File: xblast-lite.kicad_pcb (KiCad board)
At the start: 2 copper layers, 52 x 50.5 mm, 30 parts, among them J1 JTAG, J2 XBOX LPC, J3 GPIO, J4 LCD, J5 PLCC-32 Socket, Q1 BC846, Q2 BC846, U1 74LVC125, U3 XC9572XL-xxVQx44, U4 TPS27081A

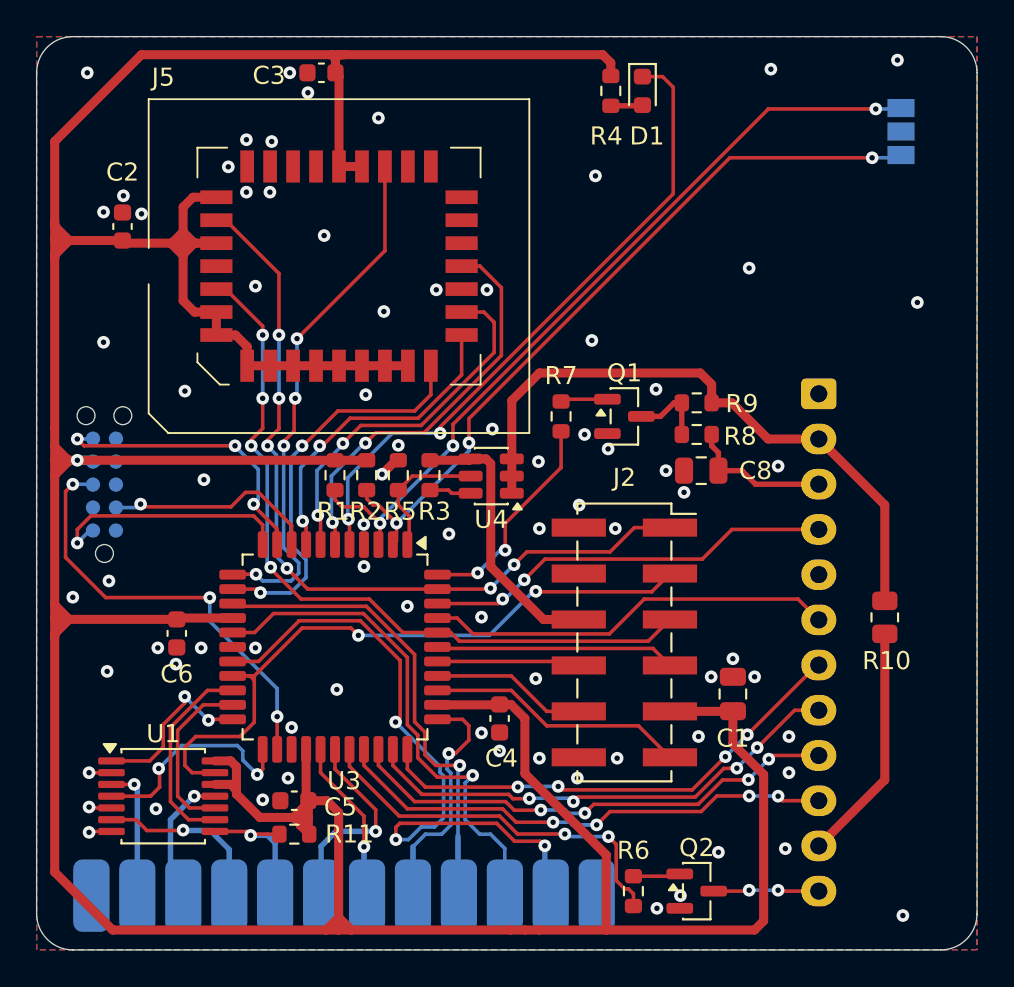
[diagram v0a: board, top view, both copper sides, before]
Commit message: Add teardrops
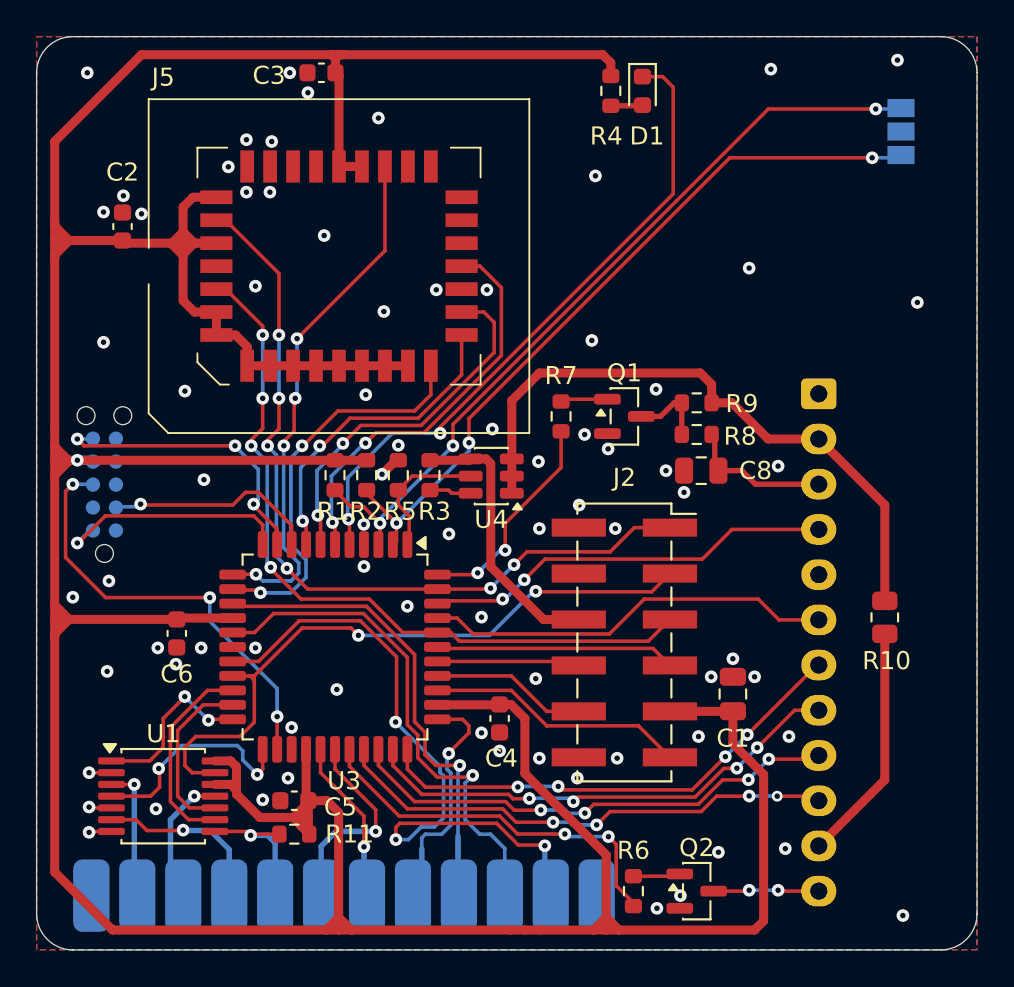
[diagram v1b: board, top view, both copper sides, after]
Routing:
- net +3V3: track 256.1 -> 258.1 mm
- net GND: vias 77 -> 76

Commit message: Fix some traces to follow 3W rule
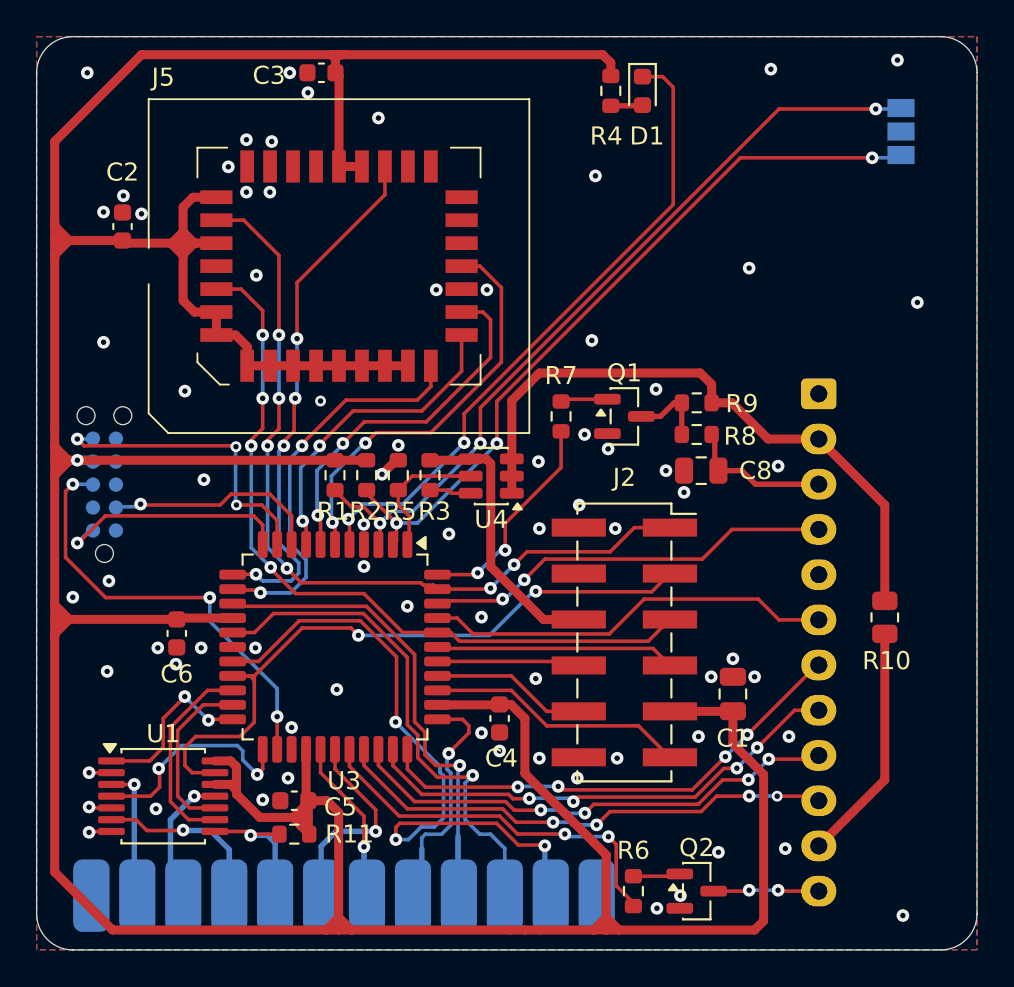
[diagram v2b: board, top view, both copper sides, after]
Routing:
- net /TMS: track 16.6 -> 17.3 mm
- net /XLCLK: track 44.8 -> 45.3 mm
- net /~{XLRESET}: track 41.8 -> 42.3 mm
- net GND: vias 76 -> 73

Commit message: Fix DRC
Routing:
- net GND: vias 73 -> 76
